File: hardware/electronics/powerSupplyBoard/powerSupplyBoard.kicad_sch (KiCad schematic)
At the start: 31 parts, among them J1 Barrel_Jack_Switch, J2 VAL, J3 VAL, J4 VAL, J9 USB_C_Receptacle_USB2.0, SW1 PTS647, SW2 SS-12D07, U4 STM32L052K6, U5 SN65HVD230QDR, U6 AP2112K-3.3, Y1 ECS-327ATQMV

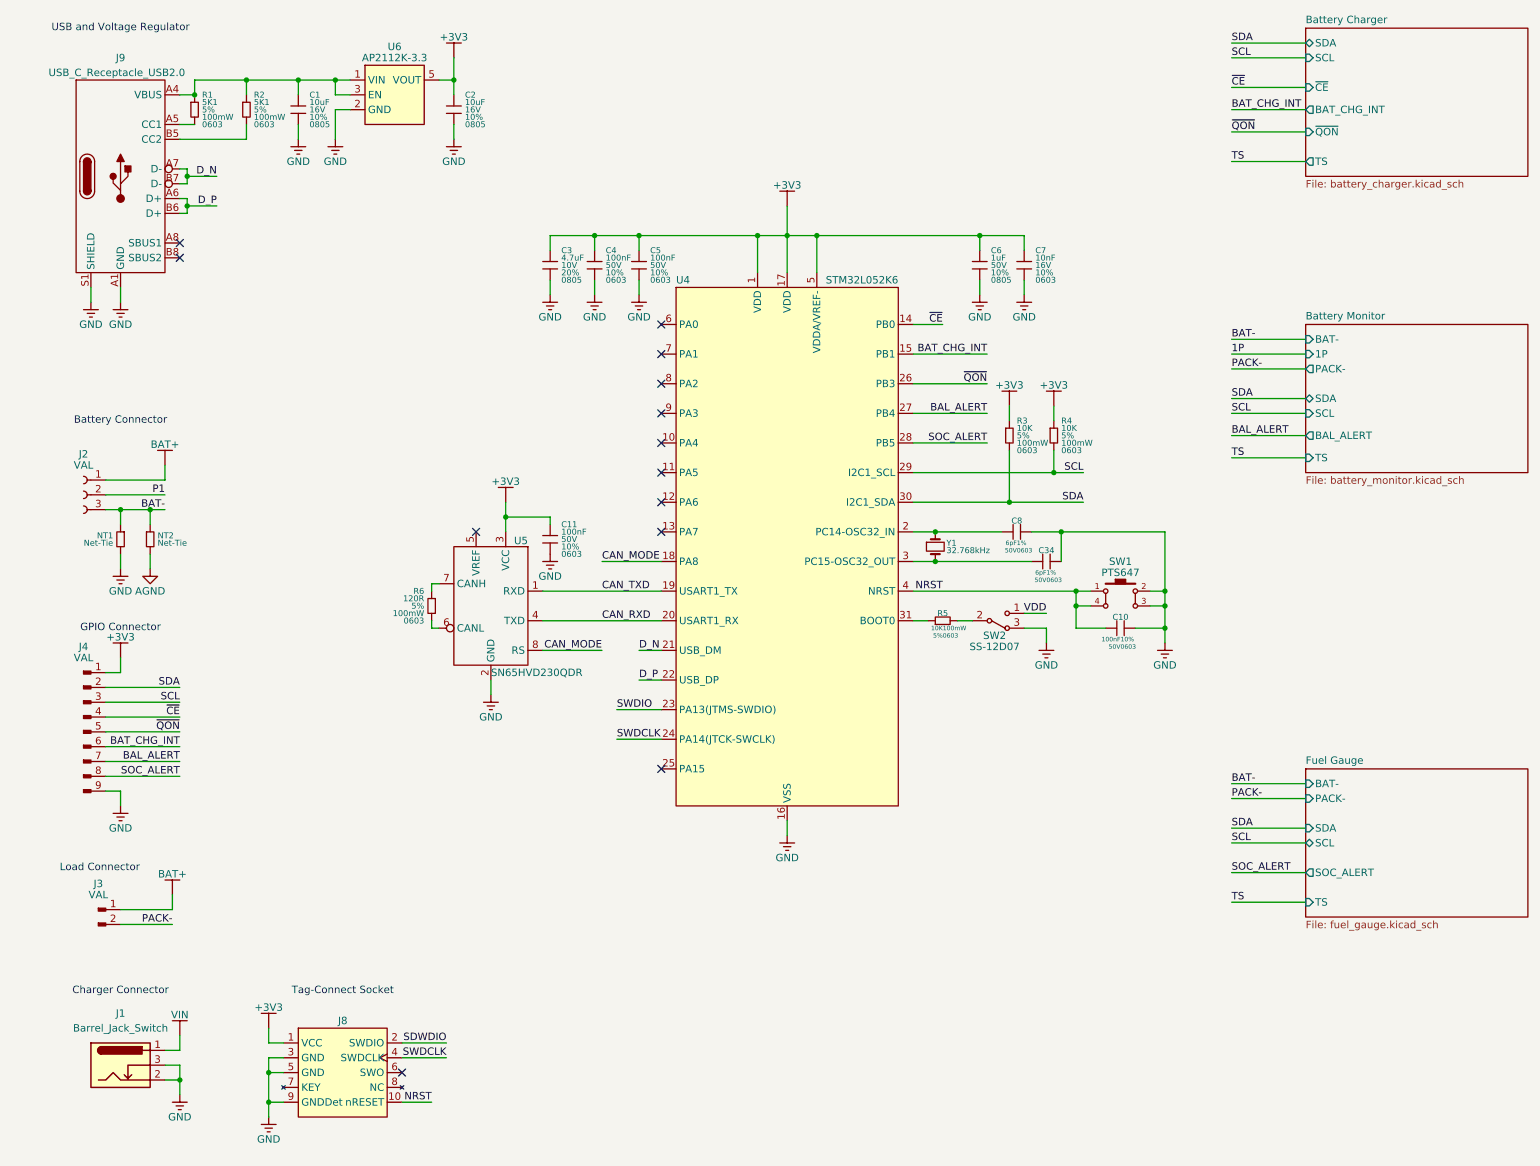
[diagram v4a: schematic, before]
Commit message: finished first page
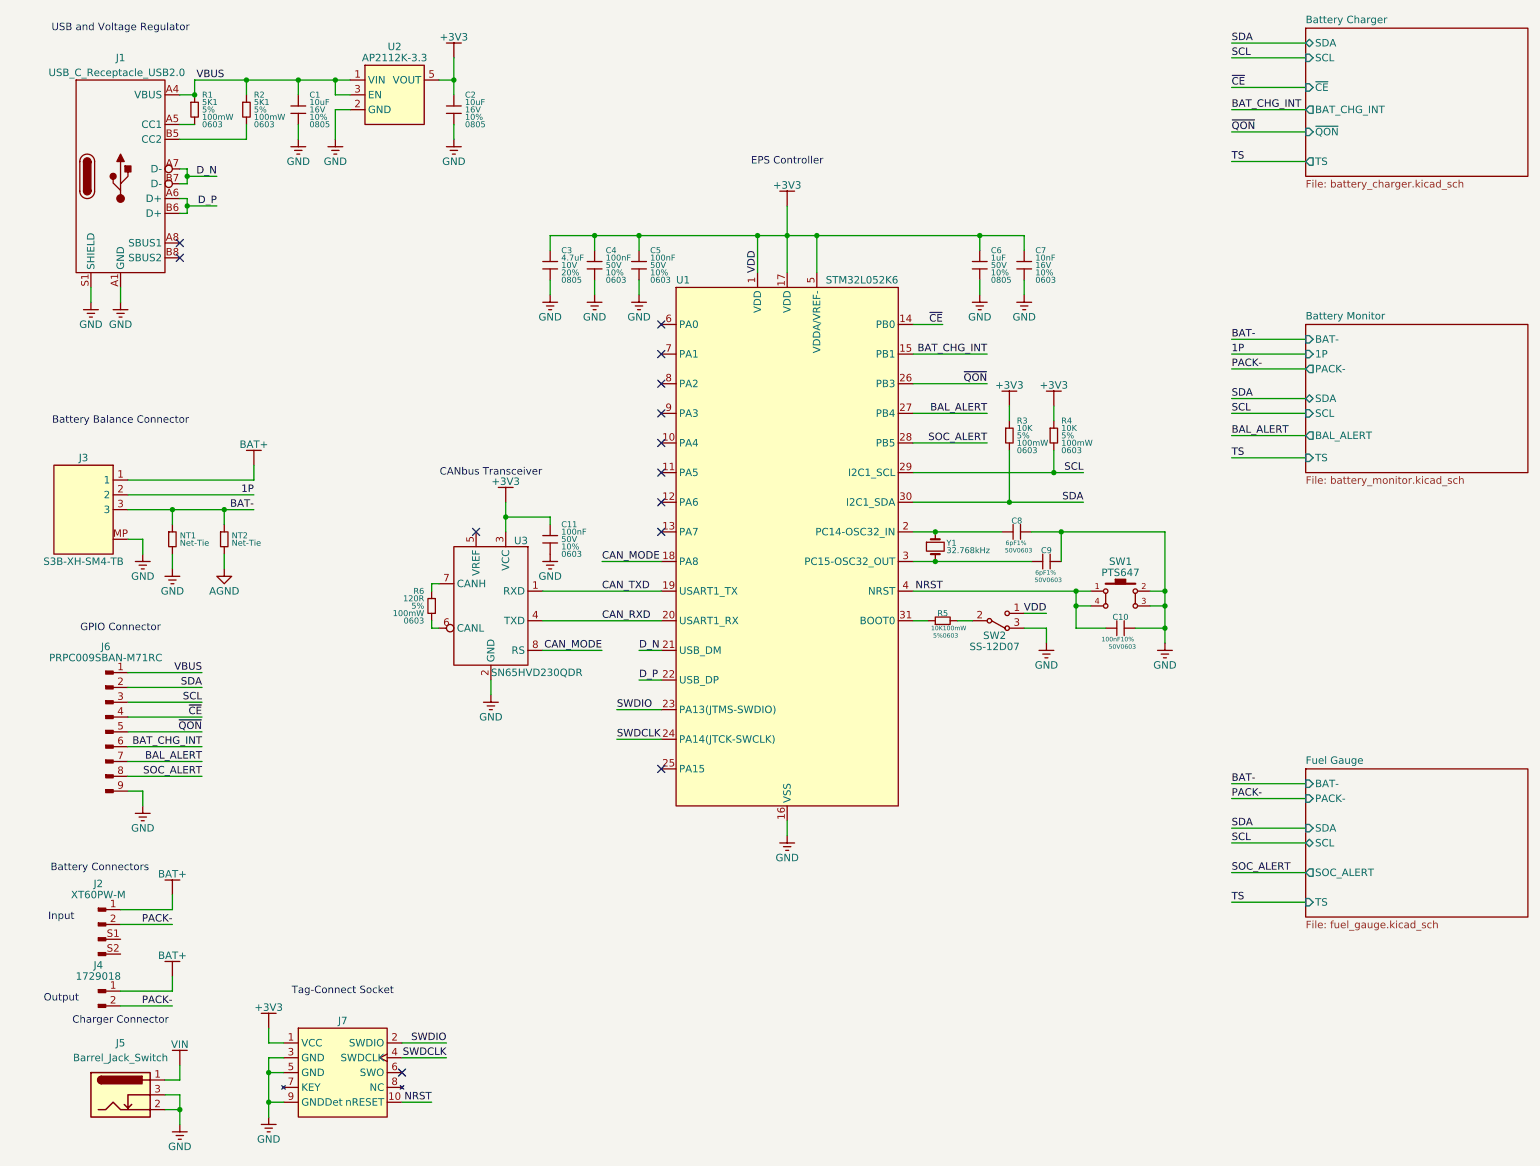
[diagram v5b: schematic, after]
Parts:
- removed J2: VAL, symbol DS-Connectors:Conn_01x03_Socket
- removed J3: VAL, symbol DS-Connectors:Conn_01x02_Pin
- removed NT2: Net-Tie, symbol DS-Passives:NT
- added J2: XT60PW-M, DS-Battery-Connectors:AMASS_XT60PW-M, symbol lib_sch:XT60PW-M
- added J3: S3B-XH-SM4-TB, DS-Rectangular-Connectors:JST_XH_S3B-SM4-TB, symbol DS-Connectors:S3B-PH-SM4-TB
- added J4: 1729018, DS-Rectangular-Connectors:5mmTerminalBlock, symbol lib_sch:Conn_01x02_Pin
- added NT2: Net-Tie, DS-Resistors-SMD:CRCW1210, symbol lib_sch:NT
- C1, C2, C6: symbol DS-Passives:C -> lib_sch:C
- C10, C8: symbol DS-Passives:C_horizontal -> lib_sch:C_horizontal
- C11, C3, C4, C5, C7: symbol DS-Passives:C -> lib_sch:C_2
- C9: renamed from C34; symbol DS-Passives:C_horizontal -> lib_sch:C_horizontal
- J1: renamed from J9; symbol DS-Connectors:USB_C_Receptacle_USB2.0 -> lib_sch:USB_C_Receptacle_USB2.0
- J5: renamed from J1; footprint (none) -> DS-Battery-Connectors:PJ-002A; symbol DS-Connectors:Barrel_Jack_Switch -> lib_sch:Barrel_Jack_Switch; DKPN (none) -> CP-002A-ND; MPN (none) -> PJ-002A; Manufacturer (none) -> Same Sky
- J6: renamed from J4; value VAL -> PRPC009SBAN-M71RC; footprint (none) -> DS-Rectangular-Connectors:conn_01x09_254_right_angle; symbol DS-Connectors:Conn_01x09_Pin -> lib_sch:Conn_01x09_Pin; DKPN (none) -> S1111EC-09-ND; MPN (none) -> PRPC009SBAN-M71RC; Manufacturer (none) -> Sullins Connector Solutions
- J7: renamed from J8; symbol DS-Connectors:JTAG-10 -> lib_sch:JTAG-10
- NT1: footprint (none) -> DS-Resistors-SMD:CRCW1210; symbol DS-Passives:NT -> lib_sch:NT; DKPN (none) -> 541-0.0WCT-ND; MPN (none) -> CRCW20100000Z0EF; Manufacturer (none) -> Vishay Dale
- R1, R2, R3, R4, R6: symbol DS-Passives:R -> lib_sch:R
- R5: symbol DS-Passives:R_horizontal -> lib_sch:R_horizontal
- SW1: symbol DS-Switches:SPST-NO Button -> lib_sch:SPST-NO Button
- SW2: footprint (none) -> DS-Switches:SS-12D07-VG_GA_PA; symbol DS-Switches:SPDT -> lib_sch:SPDT
- U1: renamed from U4; symbol DS-Micocontrollers:STM32L052K6 -> lib_sch:STM32L052K6
- U2: renamed from U6; symbol DS-PMIC:AP2112K -> lib_sch:AP2112K
- U3: renamed from U5; symbol DS-ICs:SN65HVD23xQ -> lib_sch:SN65HVD23xQ
- Y1: symbol DS-Crystals-Oscillators-Resonators:crystal_small -> lib_sch:crystal_small
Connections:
- net SDWDIO is gone; now on net SWDIO: J7.2 (SWDIO)
- net VDD is gone; now on net +3V3: SW2.1
- net +3V3: no longer J6.1
- net 1P: now also J3.2
- net AGND: now also NT2.2
- net BAT+: now also J2.1, J3.1, J4.1
- net BAT-: now also J3.3, NT2.1
- net GND: now also J3.MP
- net PACK-: now also J2.2, J4.2
- net VBUS: now reaches C1.1, J1.A4 (VBUS), J1.A9 (VBUS), J1.B4 (VBUS), J1.B9 (VBUS), R1.1, R2.1, U2.1 (VIN), U2.3 (EN)
- net VBUS: now also J6.1
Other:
- note added: "Battery Balance Connector"
- note added: "Battery Connectors"
- note added: "CANbus Transceiver"
- note added: "EPS Controller"
- note added: "Input"
- note added: "Output"
- note removed: "Battery Connector"
- note removed: "Load Connector"
- moved on the sheet: J5, J6, NT1

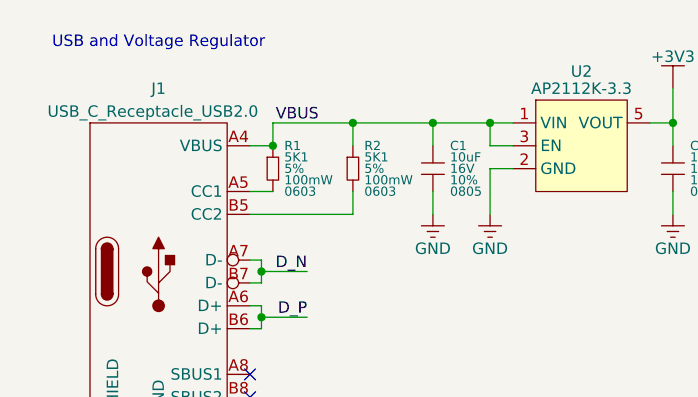
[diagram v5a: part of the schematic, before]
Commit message: fixed VUSB net label
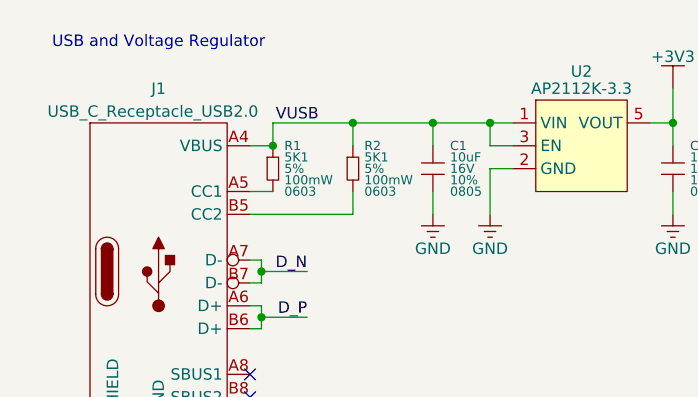
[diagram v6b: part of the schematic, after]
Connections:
- net VBUS: no longer C1.1, J1.A4 (VBUS), J1.A9 (VBUS), J1.B4 (VBUS), J1.B9 (VBUS), R1.1, R2.1, U2.1 (VIN), U2.3 (EN)
- new net VUSB: C1.1, J1.A4 (VBUS), J1.A9 (VBUS), J1.B4 (VBUS), J1.B9 (VBUS), R1.1, R2.1, U2.1 (VIN), U2.3 (EN)
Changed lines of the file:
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@@
 		)
 	)
-	(label "VBUS"
+	(label "VUSB"
 		(at 43.18 21.59 180)
 		(fields_autoplaced yes)

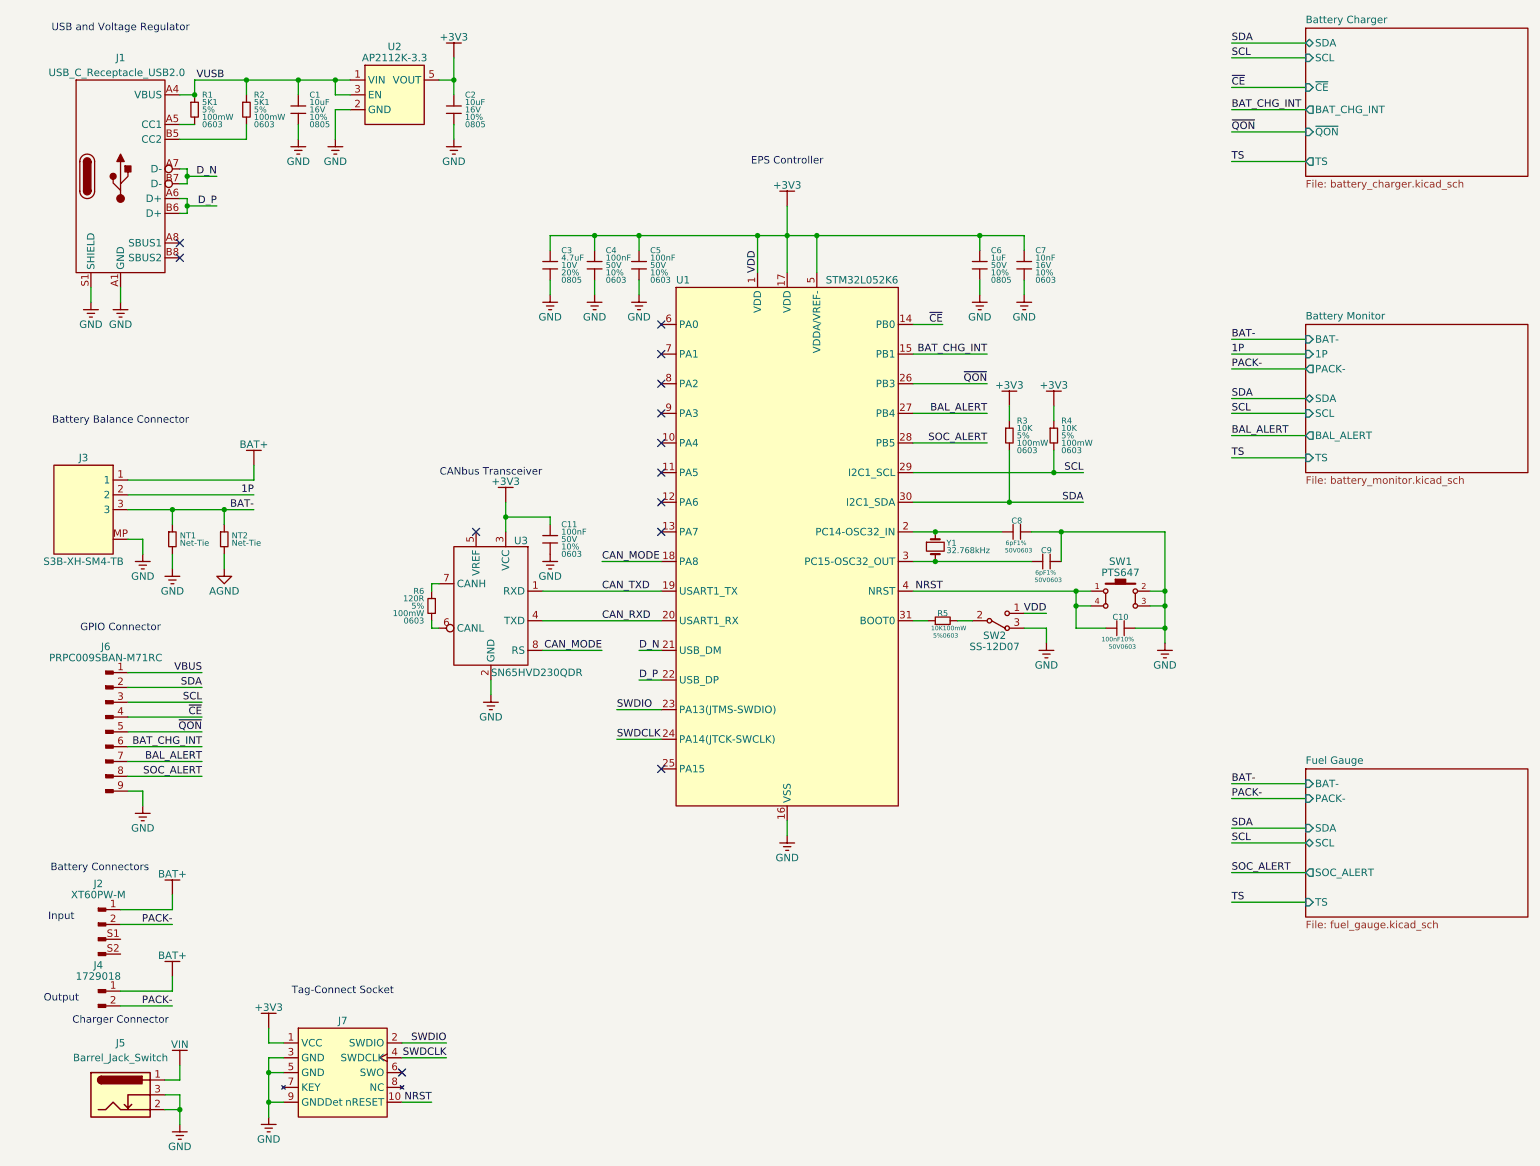
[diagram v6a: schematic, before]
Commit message: finished schematics, organized pages, and fixed ground nets
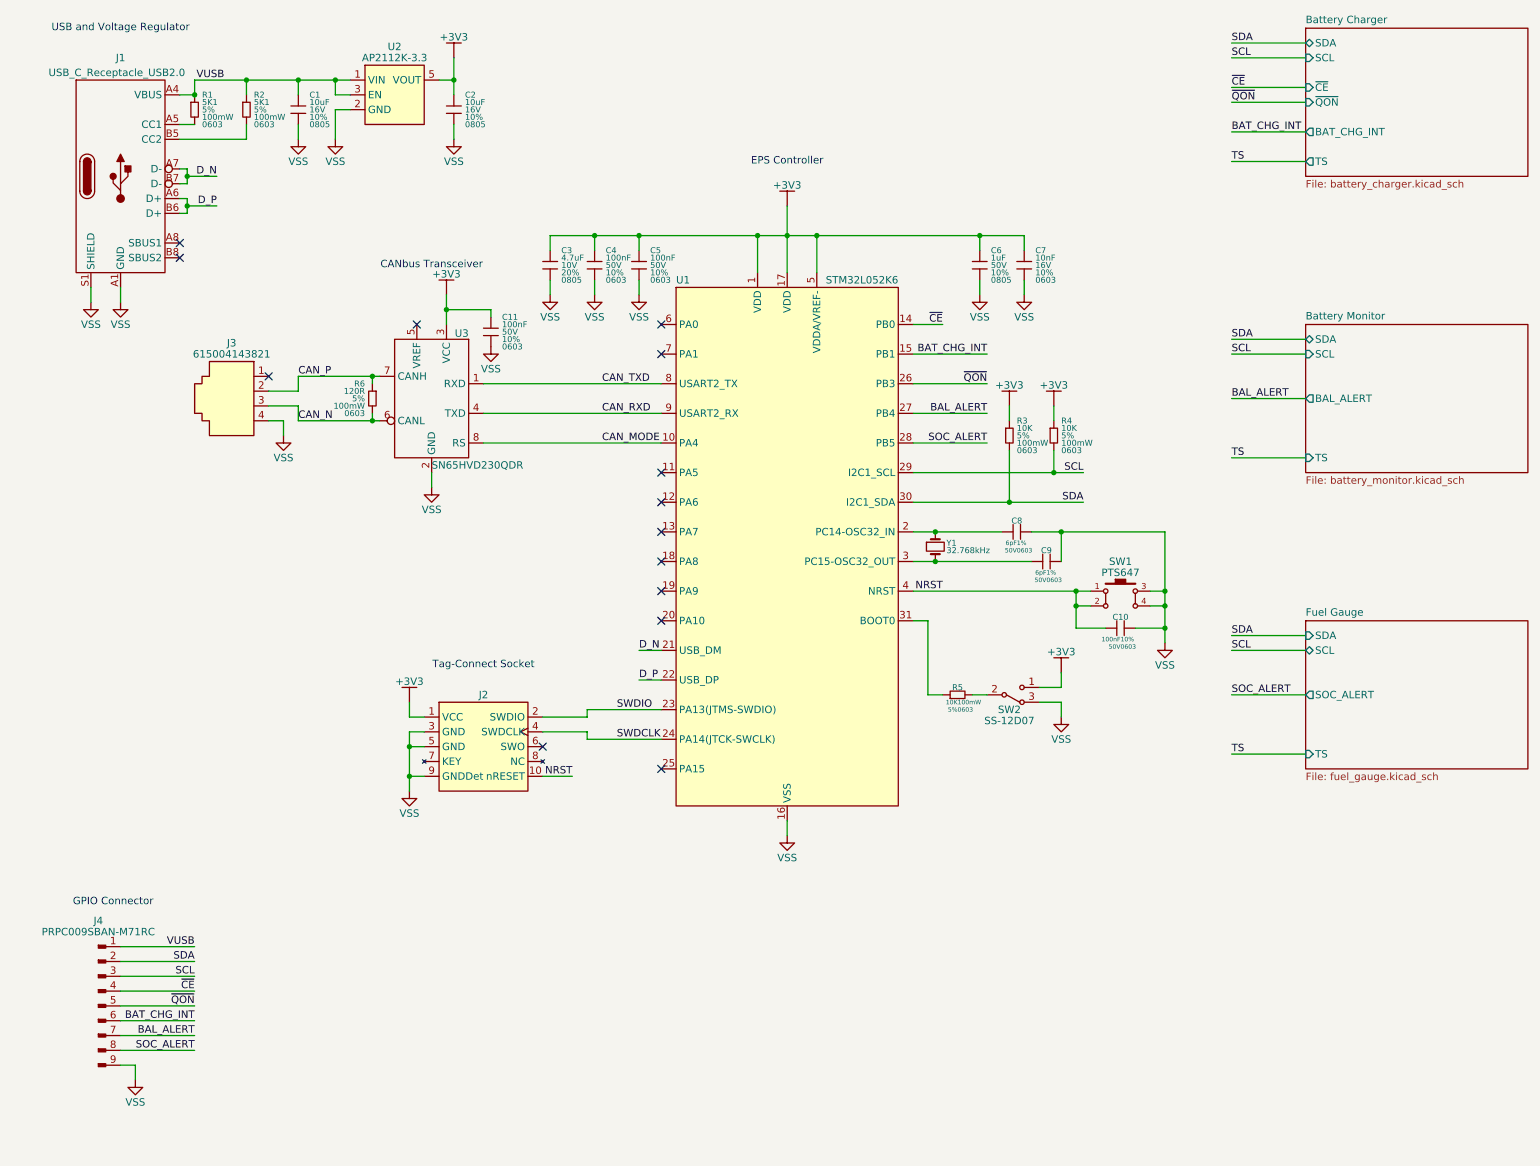
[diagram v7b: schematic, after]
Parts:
- removed J2: XT60PW-M, DS-Battery-Connectors:AMASS_XT60PW-M, symbol lib_sch:XT60PW-M
- removed J3: S3B-XH-SM4-TB, DS-Rectangular-Connectors:JST_XH_S3B-SM4-TB, symbol DS-Connectors:S3B-PH-SM4-TB
- removed J4: 1729018, DS-Rectangular-Connectors:5mmTerminalBlock, symbol lib_sch:Conn_01x02_Pin
- removed J5: Barrel_Jack_Switch, DS-Battery-Connectors:PJ-002A, symbol lib_sch:Barrel_Jack_Switch
- removed NT1, NT2: Net-Tie, DS-Resistors-SMD:CRCW1210, symbol lib_sch:NT
- added J3: 615004143821, DS-Connectors-Network:615004143821, symbol lib_sch:RJ11
- SW1: DKPN PTS647SM38SMTR2LFSCT-ND -> (none); MPN PTS 647 SM38 SMTR2 LFS -> (none); Manufacturer C&K -> (none)
- renumbered J7 to J2, J6 to J4
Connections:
- net VBUS is gone; now on net VUSB: J4.1
- net CAN_MODE: now also U1.10 (PA4); no longer U1.18 (PA8)
- net CAN_RXD: now also U1.9 (PA3); no longer U1.20 (PA10)
- net CAN_TXD: now also U1.8 (PA2); no longer U1.19 (PA9)
- net NRST: now also SW1.2; no longer SW1.4
- net CAN_N: now reaches R6.2, U3.6 (CANL)
- net CAN_N: now also J3.3
- net CAN_P: now reaches R6.1, U3.7 (CANH)
- net CAN_P: now also J3.2
- net GND renamed VSS
- net VSS: now also SW1.4, J3.4; no longer SW1.2
- no-connect marks 13 -> 14
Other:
- sheet Battery Monitor ports: added none; removed 1P, BAT-, PACK-
- sheet Fuel Gauge ports: added none; removed BAT-, PACK-
- note removed: "Battery Balance Connector"
- note removed: "Battery Connectors"
- note removed: "Charger Connector"
- note removed: "Input"
- note removed: "Output"
- moved on the sheet: C11, J2, J4, R5, R6, SW2, U3
